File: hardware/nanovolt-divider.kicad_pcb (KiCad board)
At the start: 2 copper layers, 60 x 69.1 mm, 68 parts, among them J1 NORMAL IN +, J2 NORMAL IN -, J5 DIVIDER OUT HI, J6 DIVIDER OUT LO, J7 ESP32_DISP_P1, J8 ESP32_DISP_CN1, K1 TQ2-L2-5V, K2 TQ2-L2-5V, K3 TQ2-L2-5V, K4 TQ2-L2-5V, K5 TQ2-L2-5V, Q1 MMBT2222A, Q10 MMBT2222A, Q2 MMBT2222A, Q3 MMBT2222A, Q4 MMBT2222A, Q5 MMBT2222A, Q6 MMBT2222A, Q7 MMBT2222A, Q8 MMBT2222A, Q9 MMBT2222A, U1 MCP23017-E/SO, U2 TMP275AIDR

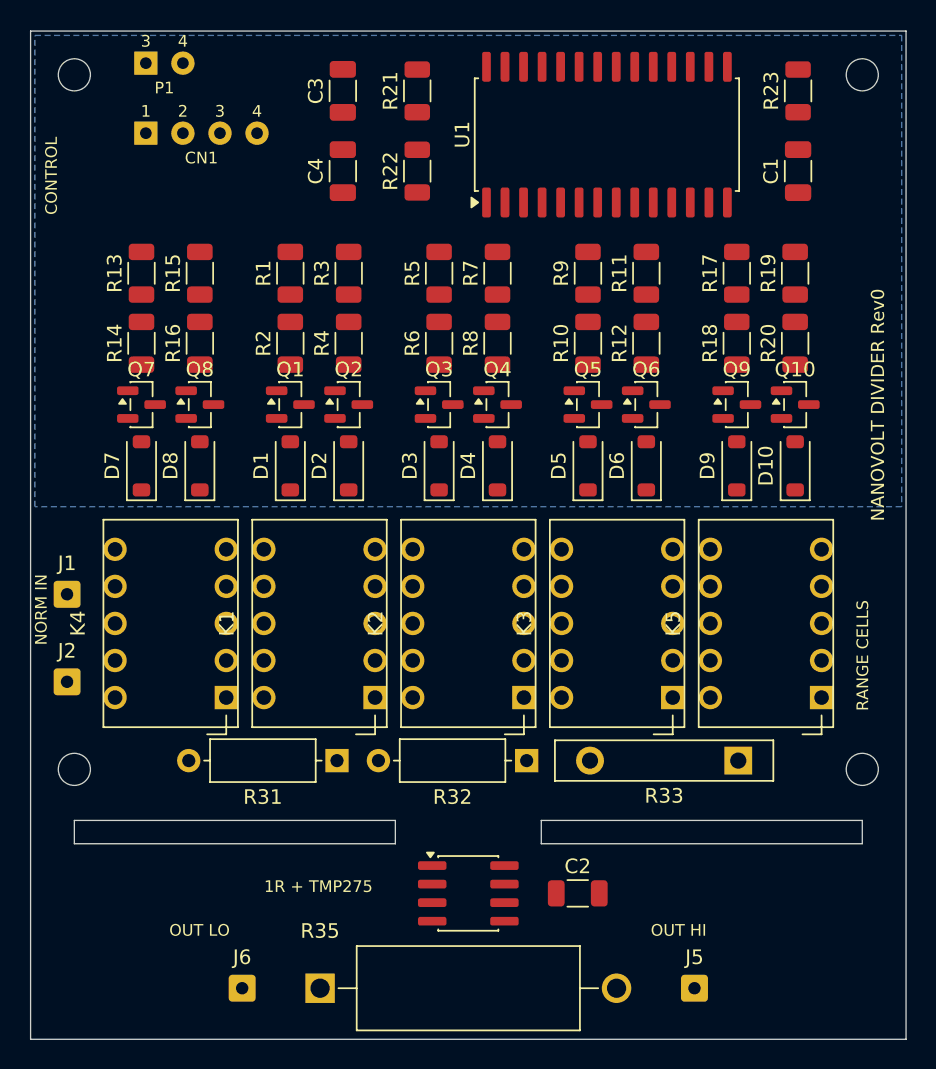
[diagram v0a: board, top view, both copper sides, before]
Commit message: Route the board: first pass, DRC 0 errors / 0 unconnected
The precision path and anything with design intent is laid by hand in
tools/route_hand.py; a grid maze router (tools/route_pcb.py) fills in the
rest around it. DRC goes from 140 unconnected to 0, with 0 errors. The 64
silk_over_copper warnings are the same set the unrouted board had.

  MEAS_NODE / ANALOG_RTN  one tight B.Cu pair, K5 to R35, via-free. RTN faces
                          the high-leg pads and takes their surface leakage.
                          It splits only under R35, along its axis.
  R35                     injection current lands on the pads from inside,
                          J5/J6 sense leaves them outside and carries none.
  HIGH vs LOWS            0.5 mm same-layer clearance between SRC_P/R*_IN and
                          RANGE_BUS/R*_OUT/MEAS_NODE; crossings on opposite
                          layers. Leakage between them shunts the high leg.
  1 ohm island            reached over the centre bridge only, no vias on it.
                          An edge-bridge track heats one end of R35: thermal
                          EMF. The first pass had put the TMP275 lines there.
  TMP275                  SDA/SCL/DGND/+3V3 as one F.Cu spine through K2.
  Drivers, coils          one cell template x10, one coil crossing x5.

R1-R20 go from 90 to 270 degrees (board and gen_pcb.py): pad 1 on top, so
the base node runs straight from the 1k to the 10k instead of past the MCP
line's pad. No part moves.

The MCP23017 fan-out is the router's work and untidy (K4_SET: 6 vias);
listed in Open items for a hand pass, along with the silkscreen.

Co-Authored-By: Claude Opus 5 <noreply@anthropic.com>
Claude-Session: https://claude.ai/code/session_0128rWrsZDfCzkxQ1CZFxeXp
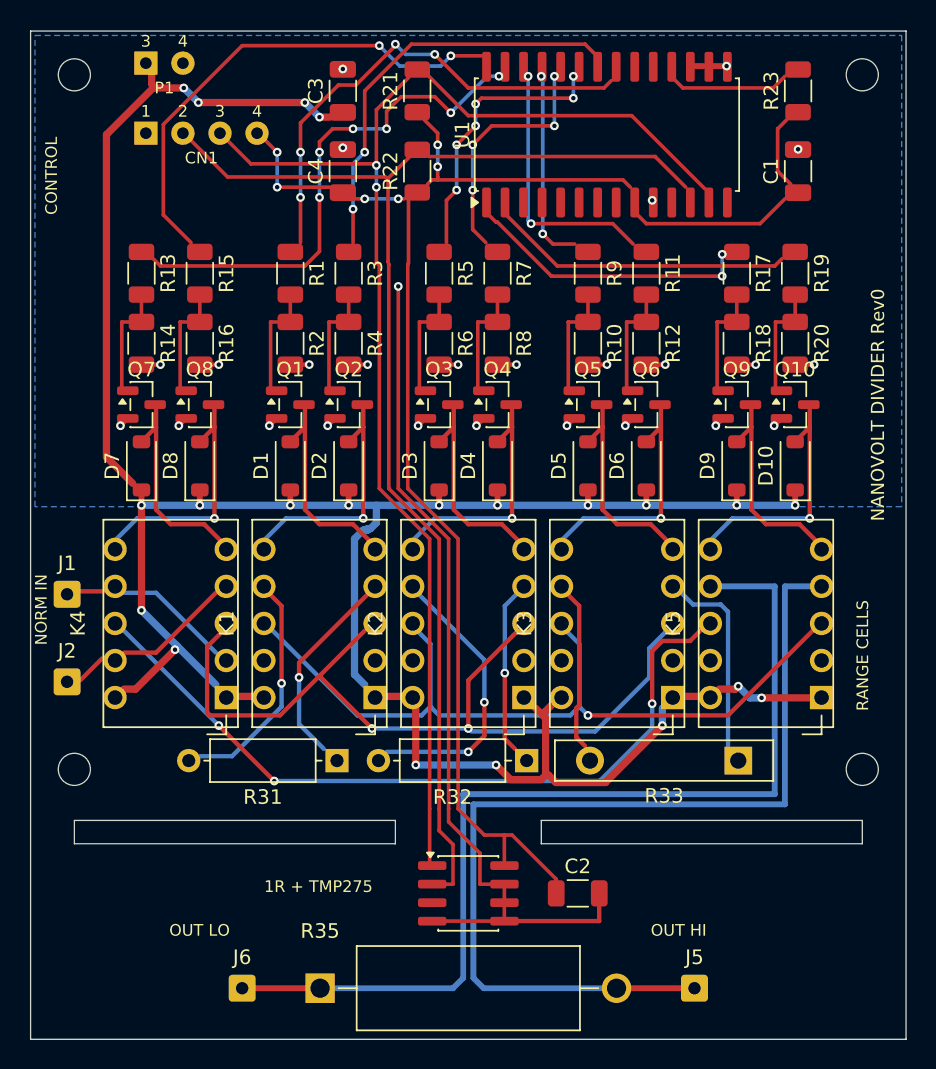
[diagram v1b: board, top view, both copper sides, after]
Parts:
- turned R1 to -90 degrees
- turned R10 to -90 degrees
- turned R11 to -90 degrees
- turned R12 to -90 degrees
- turned R13 to -90 degrees
- turned R14 to -90 degrees
- turned R15 to -90 degrees
- turned R16 to -90 degrees
- turned R17 to -90 degrees
- turned R18 to -90 degrees
- turned R19 to -90 degrees
- turned R2 to -90 degrees
- turned R20 to -90 degrees
- turned R3 to -90 degrees
- turned R4 to -90 degrees
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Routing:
- net +5V: track 0.00 -> 170.8 mm, vias 0 -> 21
- net +3V3: track 0.00 -> 100.2 mm, vias 0 -> 6
- net /CONTROL/SDA: track 0.00 -> 89.1 mm, vias 0 -> 2
- net /CONTROL/SCL: track 0.00 -> 86.8 mm
- net DGND: track 0.00 -> 82.2 mm, vias 0 -> 26
- net /ANALOG_RTN: track 0.00 -> 68.0 mm
- net /MEAS_NODE: track 0.00 -> 66.1 mm
- net /SRC_P: track 0.00 -> 56.0 mm, vias 0 -> 2
- net /RANGE_BUS: track 0.00 -> 53.7 mm, vias 0 -> 1
- net /SRC_RTN: track 0.00 -> 51.1 mm, vias 0 -> 3
- net /K4_SET: track 0.00 -> 35.4 mm, vias 0 -> 6
- net /K4_RESET: track 0.00 -> 33.8 mm, vias 0 -> 2
- net /K1_SET: track 0.00 -> 33.2 mm, vias 0 -> 4
- net /K1_RESET: track 0.00 -> 28.0 mm, vias 0 -> 2
- net /K5_RESET: track 0.00 -> 20.4 mm
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
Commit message: Tidy silkscreen after routing: 64 -> 56 silk_over_copper warnings
Hand pass over the routed board. Copper is untouched: same 1410 mm of
track, same 101 vias, no footprint moved.

  Q1-Q8 reference designators and the J1/J2/J5/J6 value text moved off pads.
  Board labels repositioned (title, NORM IN, OUT HI, OUT LO); NORM HI and
  NORM LO added at the input pads; name / revision / author block added.

DRC: 0 errors, 0 unconnected. The 56 remaining warnings are all
silk_over_copper (silkscreen clipped by solder mask), which the fab clips
anyway; judged benign.

Co-Authored-By: Claude Opus 5 <noreply@anthropic.com>
Claude-Session: https://claude.ai/code/session_0128rWrsZDfCzkxQ1CZFxeXp
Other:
- board text added: "NORM HI"
- board text added: "NORM LO"
- board text added: "nanovolt-divider Rev A • 2026 Igor Kuvychko"
- board text removed: "NANOVOLT DIVIDER Rev0"
- board text removed: "NORM IN"
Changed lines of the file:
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@@
 			(at 0 2.12 0)
 			(layer "F.Fab")
+			(hide yes)
 			(effects
 				(font
@@
 			(at 0 2.12 0)
 			(layer "F.Fab")
+			(hide yes)
 			(effects
 				(font
@@
 		(tags "SOT TO_SOT_SMD")
 		(property "Reference" "Q1"
-			(at 0 -2.4 0)
+			(at -2.8 1.15 0)
 			(layer "F.SilkS")
 			(effects
@@
 		(tags "SOT TO_SOT_SMD")
 		(property "Reference" "Q7"
-			(at 0 -2.4 0)
+			(at -3.1 0.15 0)
 			(layer "F.SilkS")
 			(effects
@@
 		)
 		(property "Value" "NORMAL IN -"
-			(at 0 2.12 0)
+			(at -4.25 2.65 0)
 			(layer "F.Fab")
+			(hide yes)
 			(effects
 				(font
@@
 		(tags "SOT TO_SOT_SMD")
 		(property "Reference" "Q8"
-			(at 0 -2.4 0)
+			(at 2.15 -1.35 0)
 			(layer "F.SilkS")
 			(effects
@@
 		(tags "SOT TO_SOT_SMD")
 		(property "Reference" "Q3"
-			(at 0 -2.4 0)
+			(at -3 1.4 0)
 			(layer "F.SilkS")
 			(effects
@@
 		)
 		(property "Value" "NORMAL IN +"
-			(at 0 2.12 0)
+			(at -8.75 2.4 0)
 			(layer "F.Fab")
+			(hide yes)
 			(effects
 				(font
@@
 		(tags "SOT TO_SOT_SMD")
 		(property "Reference" "Q4"
-			(at 0 -2.4 0)
+			(at 2 -1.35 0)
 			(layer "F.SilkS")
 			(effects
@@
 		(tags "SOT TO_SOT_SMD")
 		(property "Reference" "Q5"
-			(at 0 -2.4 0)
+			(at -2.95 1.15 0)
 			(layer "F.SilkS")
 			(effects
@@
 		(tags "SOT TO_SOT_SMD")
 		(property "Reference" "Q2"
-			(at 0 -2.4 0)
+			(at 1.95 -1.35 0)
 			(layer "F.SilkS")
 			(effects
@@
 		(tags "SOT TO_SOT_SMD")
 		(property "Reference" "Q6"
-			(at 0 -2.4 0)
+			(at 2.05 -1.35 0)
 			(layer "F.SilkS")
 			(effects
@@
 	)
 	(gr_text "OUT LO"
-		(at 59.5 112.1 0)
+		(at 62.25 118.25 0)
 		(layer "F.SilkS")
 		(effects
@@
 	)
 	(gr_text "OUT HI"
-		(at 92.5 112.1 0)
+		(at 93.75 118.25 0)
+		(layer "F.SilkS")
+		(effects
+			(font
+				(size 0.8 0.8)
+				(thickness 0.12)
+			)
+			(justify left bottom)
+		)
+	)
+	(gr_text "NORM HI"
+		(at 51.25 90.5 90)
 		(layer "F.SilkS")
 		(effects
@@
 		)
 	)
-	(gr_text "NORM IN"
-		(at 51.2 92.1 90)
+	(gr_text "NORM LO"
+		(at 51.25 97.75 90)
 		(layer "F.SilkS")
 		(effects
@@
 		)
 	)
-	(gr_text "NANOVOLT DIVIDER Rev0"
-		(at 108.6 83.6 90)
+	(gr_text "nanovolt-divider\nRev A • 2026\nIgor Kuvychko"
+		(at 51.25 111.25 0)
 		(layer "F.SilkS")
 		(effects
 			(font
-				(size 0.9 0.9)
-				(thickness 0.135)
+				(size 1 1)
+				(thickness 0.1)
 			)
 			(justify left bottom)

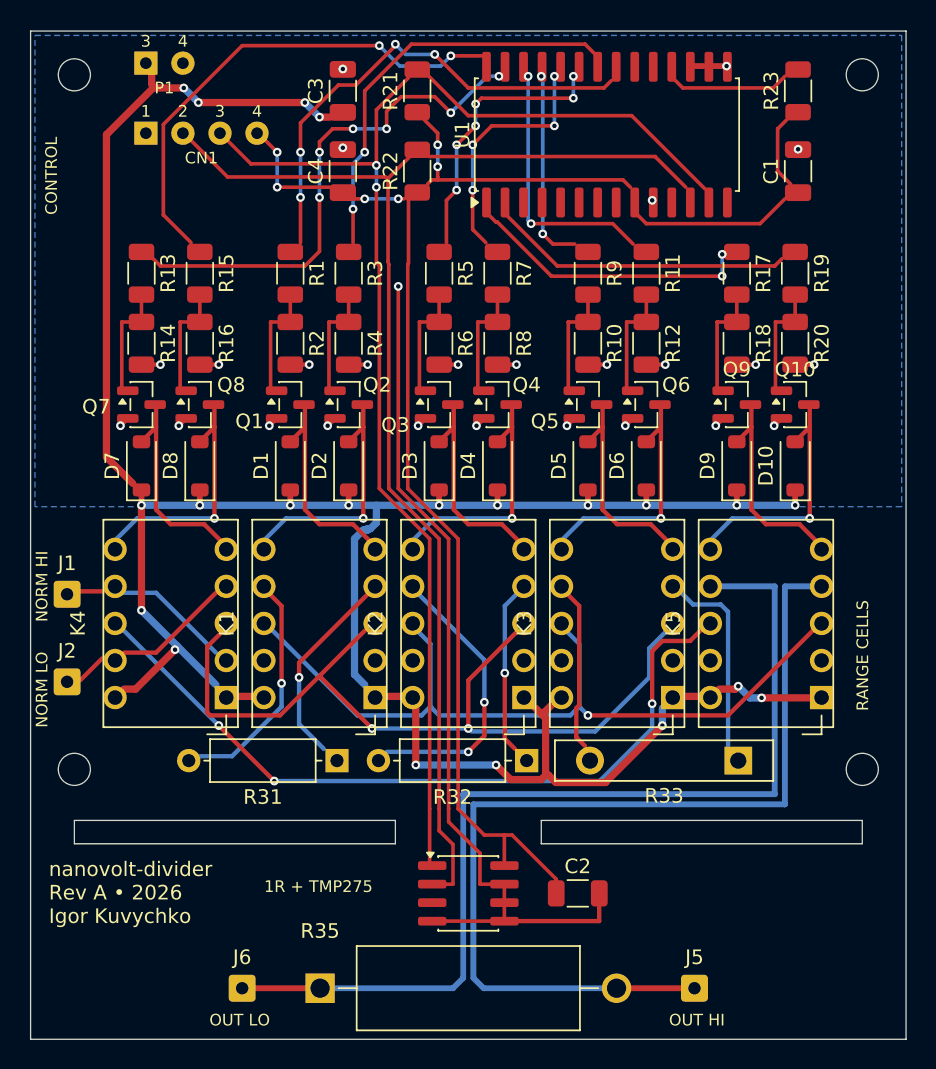
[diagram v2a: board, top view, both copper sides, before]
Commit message: Remap the MCP23017 GPIOs to the driver order: fan-out 30 vias -> 0
The coil lines were on GPA0..GPA7 (+ GPB0/1 for K5): the package row that
faces the board edge, in an order scrambled against the driver columns,
while GPB2..GPB7 - the row facing the drivers - sat unused. Every line had
to get off the wrong side of the chip and cross its neighbours.

  GPB0..GPB7  K4 S, K4 R, K1 S, K1 R, K2 S, K2 R, K3 S, K3 R  (columns' order)
  GPA0/GPA1   K5 RESET / K5 SET  (leave under the package to the right)
  GPA2..GPA7  spare

The firmware maps GPIO to coil by table; there is no firmware yet, so the
remap costs nothing there. Schematic change is in gen_schematics.py; only
control.kicad_sch changes, ERC clean, board nets synced from the netlist.

The whole control band is now hand-laid in route_hand.py: the fan-out, SDA/
SCL/3V3 under U1's body in pin order, ~RESET along the top edge, the harness
feeds between C3 and C4, +5V down the left edge, and straight B.Cu risers
from the TMP275 spine to the bus.

  MCP23017 coil lines   237 mm, 30 vias  ->  161 mm, 0 vias
  vias, whole board     101              ->  68

Also:
  route_pcb.py  vias now keep SEP from the other precision class. Two SRC_P
                vias sat 0.46 mm from RANGE_BUS; now 0 pairs under 0.5 mm.
  pcb_io.py     apply failed silently (never saved) on a board that already
                had tracks: GetNetsByName() breaks once tracks are removed.
                Look nets up with FindNet, and fail loudly if one is missing.

DRC: 0 errors, 0 unconnected, 0 schematic-parity issues, 56 benign
silk_over_copper. Silkscreen from the hand pass is untouched.

Co-Authored-By: Claude Opus 5 <noreply@anthropic.com>
Claude-Session: https://claude.ai/code/session_0128rWrsZDfCzkxQ1CZFxeXp
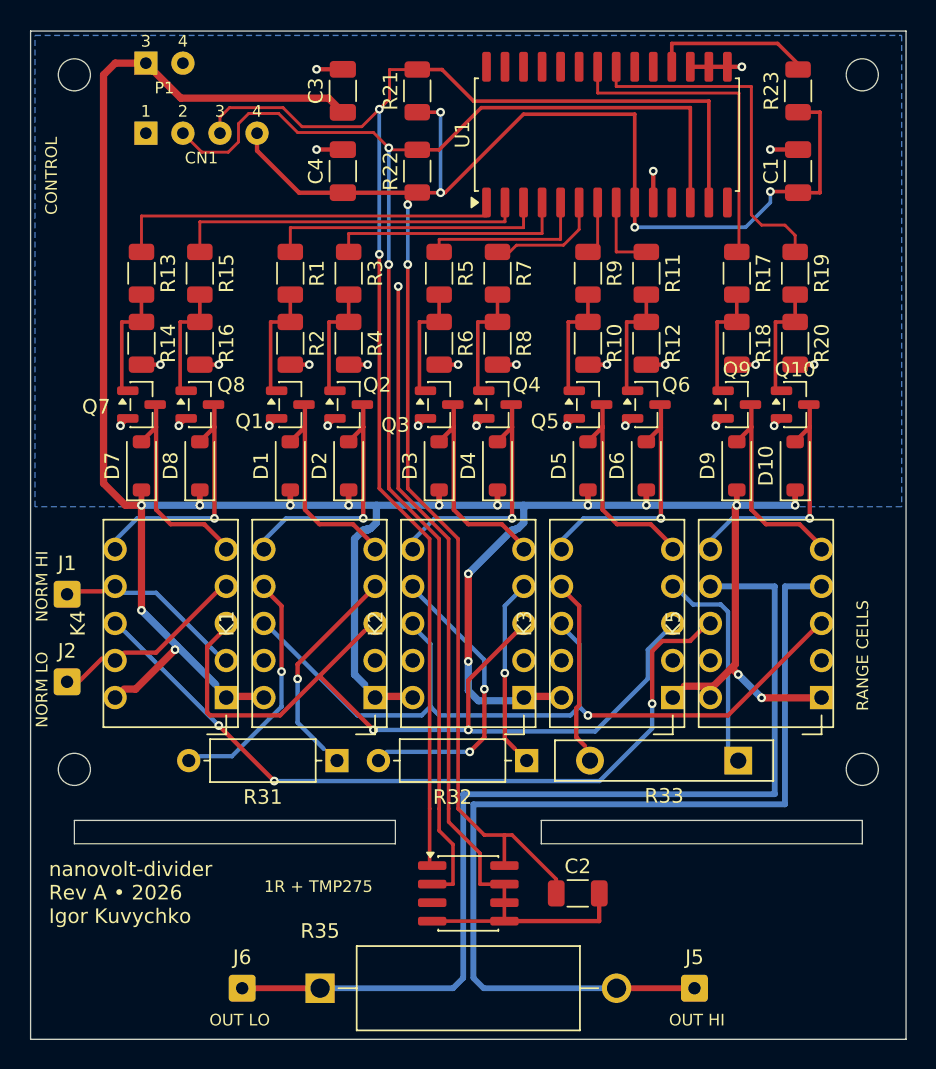
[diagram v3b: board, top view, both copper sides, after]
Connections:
- U1 pad 1: /K5_SET -> /K4_SET
- U1 pad 2: /K5_RESET -> /K4_RESET
- U1 pad 21: /K1_SET -> /K5_RESET
- U1 pad 22: /K1_RESET -> /K5_SET
- U1 pad 23: /K2_SET -> unconnected-(U1-GPA2-Pad23)
- U1 pad 24: /K2_RESET -> unconnected-(U1-GPA3-Pad24)
- U1 pad 25: /K3_SET -> unconnected-(U1-GPA4-Pad25)
- U1 pad 26: /K3_RESET -> unconnected-(U1-GPA5-Pad26)
- U1 pad 27: /K4_SET -> unconnected-(U1-GPA6-Pad27)
- U1 pad 28: /K4_RESET -> unconnected-(U1-GPA7-Pad28)
- U1 pad 3: unconnected-(U1-GPB2-Pad3) -> /K1_SET
- U1 pad 4: unconnected-(U1-GPB3-Pad4) -> /K1_RESET
- U1 pad 5: unconnected-(U1-GPB4-Pad5) -> /K2_SET
- U1 pad 6: unconnected-(U1-GPB5-Pad6) -> /K2_RESET
- U1 pad 7: unconnected-(U1-GPB6-Pad7) -> /K3_SET
- U1 pad 8: unconnected-(U1-GPB7-Pad8) -> /K3_RESET
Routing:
- net +3V3: track 100.2 -> 121.1 mm
- net /K1_SET: track 33.2 -> 19.4 mm, vias 4 -> 0
- net /K3_RESET: track 17.9 -> 4.85 mm, vias 2 -> 0
- net /CONTROL/SCL: track 86.8 -> 99.6 mm, vias 0 -> 2
- net /K1_RESET: track 28.0 -> 16.6 mm, vias 2 -> 0
- net /CONTROL/SDA: track 89.1 -> 99.3 mm
- net /K3_SET: track 13.3 -> 3.39 mm, vias 2 -> 0
- net DGND: track 82.2 -> 92.1 mm
- net /K4_RESET: track 33.8 -> 24.3 mm, vias 2 -> 0
- net /K4_SET: track 35.4 -> 26.1 mm, vias 6 -> 0
- net /K2_RESET: track 16.8 -> 8.08 mm, vias 4 -> 0
- net +5V: track 170.8 -> 179.2 mm, vias 21 -> 16
- net /K2_SET: track 18.7 -> 11.7 mm, vias 6 -> 0
- net /K5_RESET: track 20.4 -> 24.1 mm
- net Net-(U1-~{RESET}): track 8.04 -> 11.2 mm
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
